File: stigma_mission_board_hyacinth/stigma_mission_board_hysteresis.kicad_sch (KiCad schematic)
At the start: 149 parts, among them J2 Conn_02x05_Top_Bottom_Mountin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, J5 Conn_02x04_Top_Bottom, J6 Conn_02x04_Top_Bottom, J7 SMA, J8 SMA, J9 JST-GH 4Pin, Q1 DMN2056U, U1 LAN8742A, U10 MCP2562-E-SN, U11 MCP2562-E-SN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

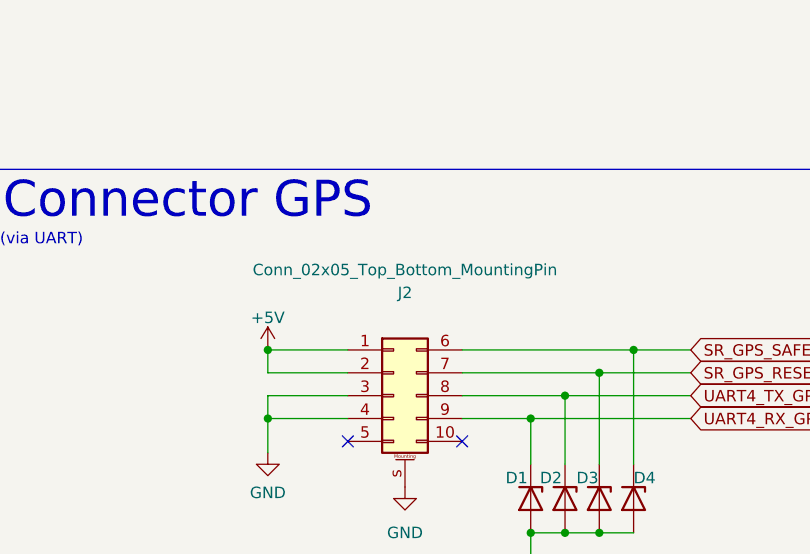
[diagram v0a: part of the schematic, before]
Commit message: added 3d models of connectors
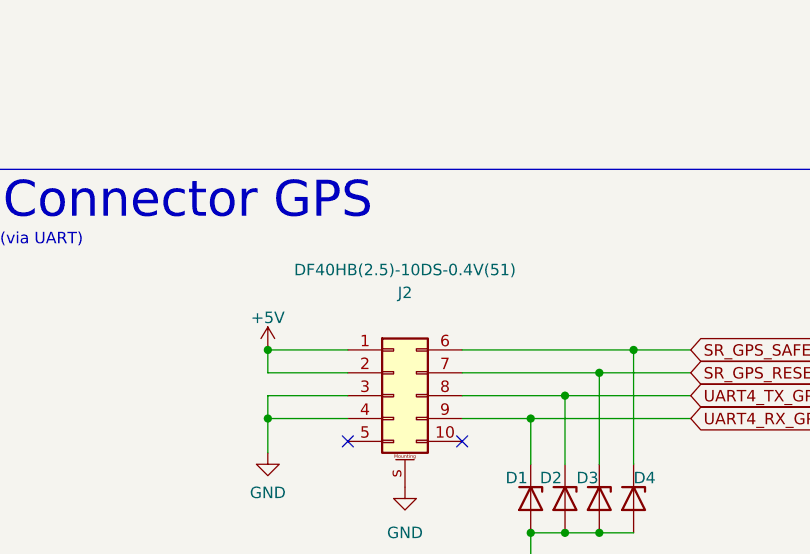
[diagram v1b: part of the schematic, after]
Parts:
- J1: value ~ -> DF40C-70DS-0.4V(51); LCSC# (none) -> C294854
- J2: value Conn_02x05_Top_Bottom_MountingPin -> DF40HB(2.5)-10DS-0.4V(51); LCSC# (none) -> C5623558
- J5, J6: value Conn_02x04_Top_Bottom -> (none)
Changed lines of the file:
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@@
 			)
 		)
-		(property "Value" "Conn_02x05_Top_Bottom_MountingPin"
+		(property "Value" "DF40HB(2.5)-10DS-0.4V(51)"
 			(at 163.83 29.21 0)
 			(effects
@@
 			)
 		)
-		(property "Datasheet" "~"
+		(property "Datasheet" "https://www.hirose.com/en/product/document?clcode=&productname=&series=DF40&documenttype=Catalog&lang=en&documentid=en_DF40_CAT"
+			(at 162.56 43.18 0)
+			(effects
+				(font
+					(size 1.27 1.27)
+				)
+				(hide yes)
+			)
+		)
+		(property "Description" "CONN RCPT 10POS SMD GOLD"
 			(at 162.56 43.18 0)
 			(effects
@@
 			)
 		)
-		(property "Description" "Generic connectable mounting pin connector, double row, 02x05, top/bottom pin numbering scheme (row 1: 1...pins_per_row, row2: pins_per_row+1 ... num_pins), script generated (kicad-library-utils/schlib/autogen/connector/)"
+		(property "LCSC#" "C5623558"
 			(at 162.56 43.18 0)
 			(effects
@@
 	)
 	(symbol
-		(lib_id "Connector_Generic:Conn_02x04_Top_Bottom")
-		(at 336.55 55.88 0)
-		(unit 1)
-		(exclude_from_sim no)
-		(in_bom yes)
-		(on_board yes)
-		(dnp no)
-		(property "Reference" "J6"
-			(at 337.82 50.546 0)
-			(effects
-				(font
-					(size 1.27 1.27)
-				)
-			)
-		)
-		(property "Value" "Conn_02x04_Top_Bottom"
-			(at 337.82 49.53 0)
-			(effects
-				(font
-					(size 1.27 1.27)
-				)
-				(hide yes)
-			)
-		)
-		(property "Footprint" "Connector_Molex:Molex_Micro-Fit_3.0_43045-0800_2x04_P3.00mm_Horizontal"
-			(at 336.55 55.88 0)
-			(effects
-				(font
-					(size 1.27 1.27)
-				)
-				(hide yes)
-			)
-		)
-		(property "Datasheet" "~"
-			(at 336.55 55.88 0)
-			(effects
-				(font
-					(size 1.27 1.27)
-				)
-				(hide yes)
-			)
-		)
-		(property "Description" "Generic connector, double row, 02x04, top/bottom pin numbering scheme (row 1: 1...pins_per_row, row2: pins_per_row+1 ... num_pins), script generated (kicad-library-utils/schlib/autogen/connector/)"
-			(at 336.55 55.88 0)
-			(effects
-				(font
-					(size 1.27 1.27)
-				)
-				(hide yes)
-			)
-		)
-		(pin "6"
-		)
-		(pin "1"
-		)
-		(pin "7"
-		)
-		(pin "2"
-		)
-		(pin "4"
-		)
-		(pin "3"
-		)
-		(pin "5"
-		)
-		(pin "8"
-		)
-		(instances
-			(project "stigma_mission_board_hysteresis"
-				(path "/34e067c7-b84e-477a-88f3-7322f422dd23"
-					(reference "J6")
-					(unit 1)
-				)
-			)
-		)
-	)
-	(symbol
 		(lib_id "Device:R")
 		(at 176.53 389.89 0)
@@
 	)
 	(symbol
-		(lib_id "Connector_Generic:Conn_02x02_Top_Bottom")
-		(at 335.28 113.03 0)
-		(unit 1)
-		(exclude_from_sim no)
-		(in_bom yes)
-		(on_board yes)
-		(dnp no)
-		(property "Reference" "J4"
-			(at 336.296 110.744 0)
-			(effects
-				(font
-					(size 1.27 1.27)
-				)
-			)
-		)
-		(property "Value" "~"
-			(at 335.026 109.474 0)
-			(effects
-				(font
-					(size 1.27 1.27)
-				)
-				(hide yes)
-			)
-		)
-		(property "Footprint" "Connector_Molex:Molex_Micro-Fit_3.0_43045-0400_2x02_P3.00mm_Horizontal"
-			(at 335.28 113.03 0)
-			(effects
-				(font
-					(size 1.27 1.27)
-				)
-				(hide yes)
-			)
-		)
-		(property "Datasheet" "~"
-			(at 335.28 113.03 0)
-			(effects
-				(font
-					(size 1.27 1.27)
-				)
-				(hide yes)
-			)
-		)
-		(property "Description" "Generic connector, double row, 02x02, top/bottom pin numbering scheme (row 1: 1...pins_per_row, row2: pins_per_row+1 ... num_pins), script generated (kicad-library-utils/schlib/autogen/connector/)"
-			(at 335.28 113.03 0)
-			(effects
-				(font
-					(size 1.27 1.27)
-				)
-				(hide yes)
-			)
-		)
-		(pin "3"
-		)
-		(pin "2"
-		)
-		(pin "4"
-		)
-		(pin "1"
-		)
-		(instances
-			(project "stigma_mission_board_hysteresis"
-				(path "/34e067c7-b84e-477a-88f3-7322f422dd23"
-					(reference "J4")
-					(unit 1)
-				)
-			)
-		)
-	)
-	(symbol
 		(lib_id "Device:R")
 		(at 148.59 341.63 0)
@@
 			)
 		)
-		(property "Datasheet" "~"
+		(property "Datasheet" ""
 			(at 335.28 93.98 0)
 			(effects
@@
 			)
 		)
-		(property "Description" "Generic connector, double row, 02x02, top/bottom pin numbering scheme (row 1: 1...pins_per_row, row2: pins_per_row+1 ... num_pins), script generated (kicad-library-utils/schlib/autogen/connector/)"
+		(property "Description" ""
 			(at 335.28 93.98 0)
 			(effects
@@
 			)
 		)
-		(property "Value" "~"
+		(property "Value" "DF40C-70DS-0.4V(51)"
 			(at 66.0401 50.8 90)
 			(effects
@@
 			)
 		)
-		(property "Datasheet" "~"
+		(property "Datasheet" "https://www.hirose.com/en/product/document?clcode=&productname=&series=DF40&documenttype=Catalog&lang=en&documentid=en_DF40_CAT"
 			(at 66.04 74.93 0)
 			(effects
@@
 			)
 		)
+		(property "LCSC#" "C294854"
+			(at 66.04 74.93 0)
+			(effects
+				(font
+					(size 1.27 1.27)
+				)
+				(hide yes)
+			)
+		)
 		(pin "36"
 		)
@@
 			)
 		)
-		(property "Value" "Conn_02x04_Top_Bottom"
+		(property "Value" ""
 			(at 337.82 34.29 0)
 			(effects
@@
 			)
 		)
-		(property "Datasheet" "~"
+		(property "Datasheet" ""
 			(at 336.55 40.64 0)
 			(effects
@@
 			)
 		)
-		(property "Description" "Generic connector, double row, 02x04, top/bottom pin numbering scheme (row 1: 1...pins_per_row, row2: pins_per_row+1 ... num_pins), script generated (kicad-library-utils/schlib/autogen/connector/)"
+		(property "Description" ""
 			(at 336.55 40.64 0)
 			(effects
@@
 	)
 	(symbol
+		(lib_id "Connector_Generic:Conn_02x02_Top_Bottom")
+		(at 335.28 113.03 0)
+		(unit 1)
+		(exclude_from_sim no)
+		(in_bom yes)
+		(on_board yes)
+		(dnp no)
+		(property "Reference" "J4"
+			(at 336.296 110.744 0)
+			(effects
+				(font
+					(size 1.27 1.27)
+				)
+			)
+		)
+		(property "Value" "~"
+			(at 335.026 109.474 0)
+			(effects
+				(font
+					(size 1.27 1.27)
+				)
+				(hide yes)
+			)
+		)
+		(property "Footprint" "Connector_Molex:Molex_Micro-Fit_3.0_43045-0400_2x02_P3.00mm_Horizontal"
+			(at 335.28 113.03 0)
+			(effects
+				(font
+					(size 1.27 1.27)
+				)
+				(hide yes)
+			)
+		)
+		(property "Datasheet" ""
+			(at 335.28 113.03 0)
+			(effects
+				(font
+					(size 1.27 1.27)
+				)
+				(hide yes)
+			)
+		)
+		(property "Description" ""
+			(at 335.28 113.03 0)
+			(effects
+				(font
+					(size 1.27 1.27)
+				)
+				(hide yes)
+			)
+		)
+		(pin "3"
+		)
+		(pin "2"
+		)
+		(pin "4"
+		)
+		(pin "1"
+		)
+		(instances
+			(project "stigma_mission_board_hysteresis"
+				(path "/34e067c7-b84e-477a-88f3-7322f422dd23"
+					(reference "J4")
+					(unit 1)
+				)
+			)
+		)
+	)
+	(symbol
 		(lib_id "power:GND")
 		(at 148.59 49.53 0)
@@
 					(unit 1)
 				)
+			)
+		)
+	)
+	(symbol
+		(lib_id "Connector_Generic:Conn_02x04_Top_Bottom")
+		(at 336.55 55.88 0)
+		(unit 1)
+		(exclude_from_sim no)
+		(in_bom yes)
+		(on_board yes)
+		(dnp no)
+		(property "Reference" "J6"
+			(at 337.82 50.546 0)
+			(effects
+				(font
+					(size 1.27 1.27)
+				)
+			)
+		)
+		(property "Value" ""
+			(at 337.82 49.53 0)
+			(effects
+				(font
+					(size 1.27 1.27)
+				)
+				(hide yes)
+			)
+		)
+		(property "Footprint" "Connector_Molex:Molex_Micro-Fit_3.0_43045-0800_2x04_P3.00mm_Horizontal"
+			(at 336.55 55.88 0)
+			(effects
+				(font
+					(size 1.27 1.27)
+				)
+				(hide yes)
+			)
+		)
+		(property "Datasheet" ""
+			(at 336.55 55.88 0)
+			(effects
+				(font
+					(size 1.27 1.27)
+				)
+				(hide yes)
+			)
+		)
+		(property "Description" ""
+			(at 336.55 55.88 0)
+			(effects
+				(font
+					(size 1.27 1.27)
+				)
+				(hide yes)
+			)
+		)
+		(pin "6"
+		)
+		(pin "1"
+		)
+		(pin "7"
+		)
+		(pin "2"
+		)
+		(pin "4"
+		)
+		(pin "3"
+		)
+		(pin "5"
+		)
+		(pin "8"
+		)
+		(instances
+			(project "stigma_mission_board_hysteresis"
+				(path "/34e067c7-b84e-477a-88f3-7322f422dd23"
+					(reference "J6")
+					(unit 1)
+				)

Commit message: changed pcb design. currently not working
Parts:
- removed H2, H3, H7, H8: MountingHole_Pad, MountingHole:MountingHole_3.2mm_M3_Pad_Via, symbol Mechanical:MountingHole_Pad
- J5, J6: value (none) -> ~
- renumbered H4 to H2, H5 to H3, H6 to H4, H9 to H5, H10 to H6
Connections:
- net high_current: no longer R23.1
- net high_current_2: now also R23.1
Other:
- moved on the sheet: H2, H3, H4, H5, H6

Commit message: Layed out 3.3v regulators, buzzer, shift register and current + voltage sensing on the mission board pcb
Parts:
- J1: footprint Stigma:core-board -> Stigma:core-board-inner-mounting-holes
- J2: footprint Stigma:gps-board-outer-mounting-holes -> Stigma:gps-board-only-inner-mounting-holes
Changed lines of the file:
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@@
 			)
 		)
-		(property "Footprint" "Stigma:gps-board-outer-mounting-holes"
+		(property "Footprint" "Stigma:gps-board-only-inner-mounting-holes"
 			(at 162.56 43.18 0)
 			(effects
@@
 			)
 		)
-		(property "Footprint" "Stigma:core-board"
+		(property "Footprint" "Stigma:core-board-inner-mounting-holes"
 			(at 66.04 74.93 0)
 			(effects

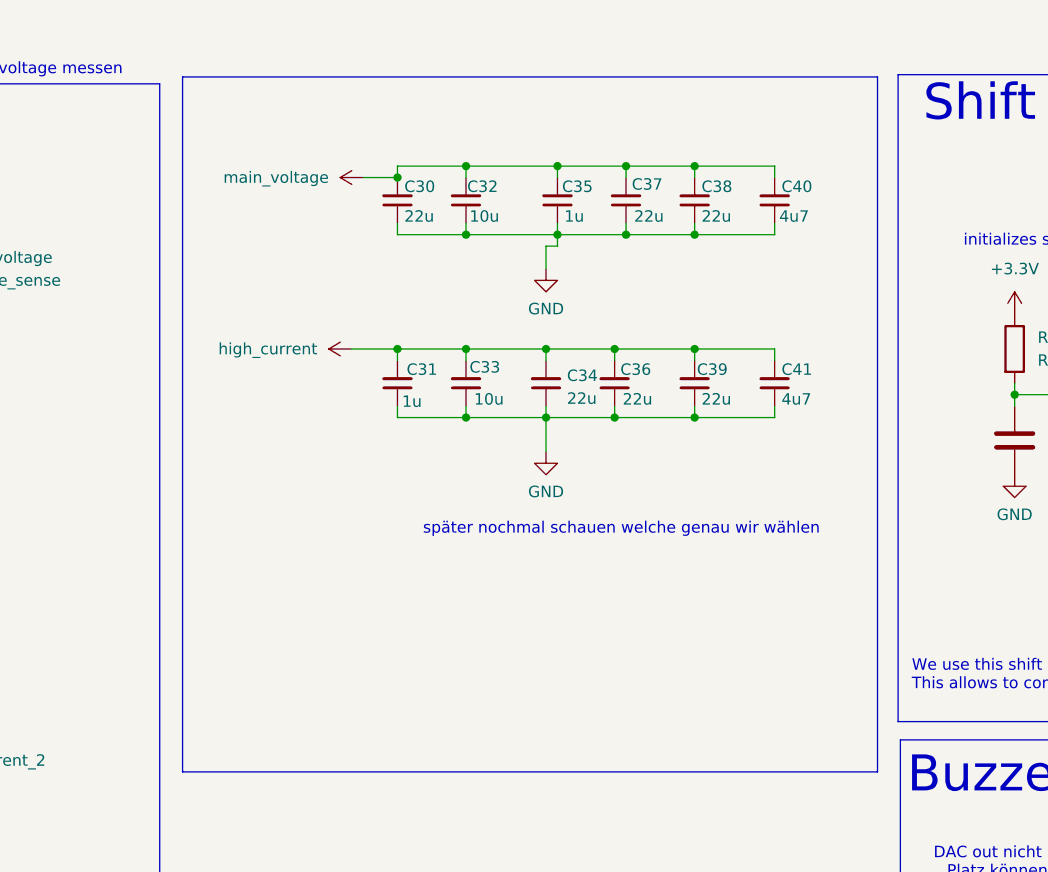
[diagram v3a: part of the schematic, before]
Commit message: changed capacitors
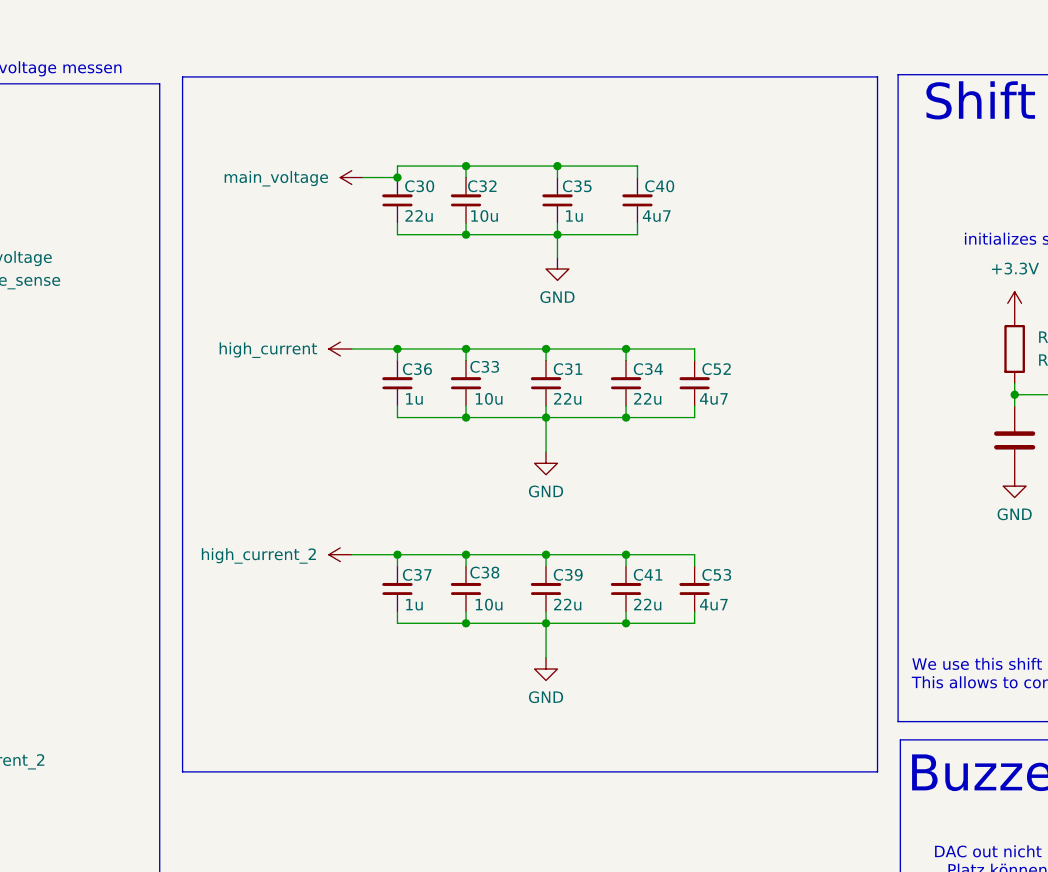
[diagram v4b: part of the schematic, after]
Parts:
- added C52, C53: 4u7, Capacitor_SMD:C_0805_2012Metric, symbol Device:C_Small
- C30, C34, C39: footprint Capacitor_SMD:C_1206_3216Metric -> Capacitor_SMD:C_0805_2012Metric; LCSC# C12891 -> C513764; Manufacturer Samsung Electro-Mechanics -> Samwha Capacitor; Part# CL31A226KAHNNNE -> CS2012X5R226M250NRE
- C31: value 1u -> 22u; footprint Capacitor_SMD:C_1206_3216Metric -> Capacitor_SMD:C_0805_2012Metric; LCSC# C12891 -> C513764; Manufacturer Samsung Electro-Mechanics -> Samwha Capacitor; Part# CL31A226KAHNNNE -> CS2012X5R226M250NRE
- C32: footprint Capacitor_SMD:C_1206_3216Metric -> Capacitor_SMD:C_0805_2012Metric; LCSC# C12891 -> C5189822; Part# CL31A226KAHNNNE -> CS2012X7R106M100NRE
- C33: footprint Capacitor_SMD:C_1206_3216Metric -> Capacitor_SMD:C_0805_2012Metric; LCSC# C12891 -> C5189822; Manufacturer Samsung Electro-Mechanics -> (none); Part# CL31A226KAHNNNE -> CS2012X7R106M100NRE
- C35: footprint Capacitor_SMD:C_1206_3216Metric -> Capacitor_SMD:C_0603_1608Metric; LCSC# C12891 -> C2918486; Manufacturer Samsung Electro-Mechanics -> Samwha Capacitor; Part# CL31A226KAHNNNE -> CS1608X5R105K250NRB
- C36, C37: value 22u -> 1u; footprint Capacitor_SMD:C_1206_3216Metric -> Capacitor_SMD:C_0603_1608Metric; LCSC# C12891 -> C2918486; Manufacturer Samsung Electro-Mechanics -> Samwha Capacitor; Part# CL31A226KAHNNNE -> CS1608X5R105K250NRB
- C38: value 22u -> 10u; footprint Capacitor_SMD:C_1206_3216Metric -> Capacitor_SMD:C_0805_2012Metric; LCSC# C12891 -> C5189822; Manufacturer Samsung Electro-Mechanics -> (none); Part# CL31A226KAHNNNE -> CS2012X7R106M100NRE
- C40: footprint Capacitor_SMD:C_1206_3216Metric -> Capacitor_SMD:C_0805_2012Metric; LCSC# C1872 -> C513766; Manufacturer Samsung Electro-Mechanics -> Samwha Capacitor; Part# CL31B475KAHNNNE -> CS2012X7R475K250NRE
- C41: value 4u7 -> 22u; footprint Capacitor_SMD:C_1206_3216Metric -> Capacitor_SMD:C_0805_2012Metric; LCSC# C1872 -> C513764; Manufacturer Samsung Electro-Mechanics -> Samwha Capacitor; Part# CL31B475KAHNNNE -> CS2012X5R226M250NRE
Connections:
- net GND: now also C52.1, C53.1
- net high_current: now also C52.2; no longer C39.2, C41.2
- net high_current_2: now also C37.2, C38.2, C39.2, C41.2, C53.2
- net main_voltage: no longer C37.2, C38.2
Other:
- note removed: "später nochmal schauen welche genau wir wählen"
- moved on the sheet: C40

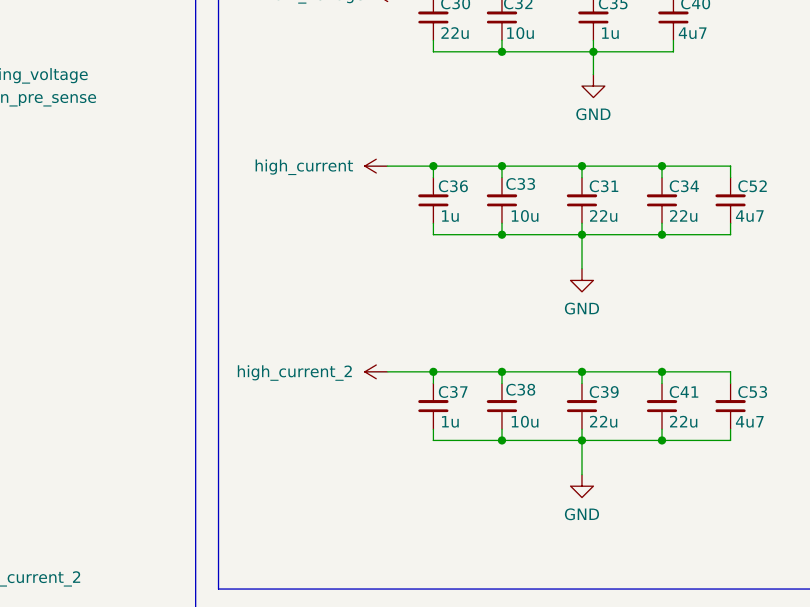
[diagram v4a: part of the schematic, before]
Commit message: added ethernet layout to pcb and changed minor errors
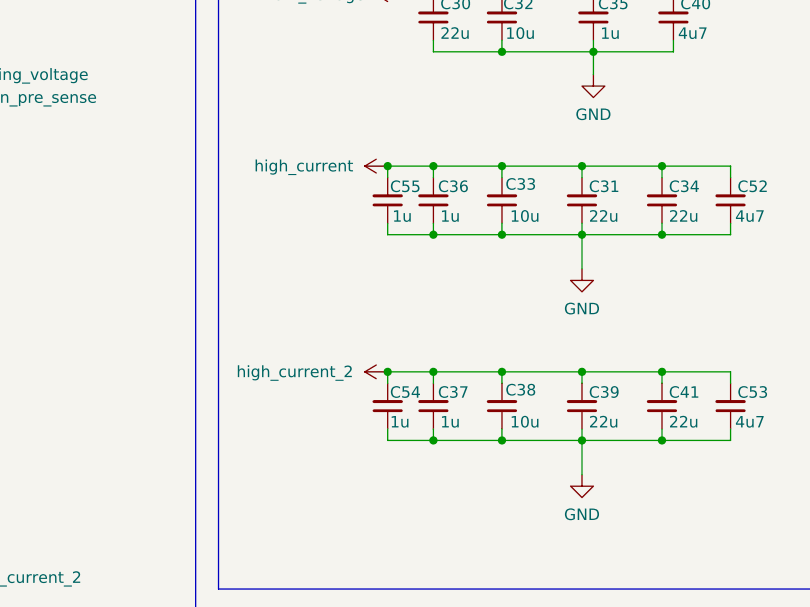
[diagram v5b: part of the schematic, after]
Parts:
- added C54, C55: 1u, Capacitor_SMD:C_0603_1608Metric, symbol Device:C_Small
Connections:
- net GND: now also C54.1, C55.1
- net high_current: now also C55.2
- net high_current_2: now also C54.2
